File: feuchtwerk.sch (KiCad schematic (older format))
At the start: 47 parts, among them P1 CONN_01X04, P2 CONN_01X08, P3 CONN_01X08, U1 STM32F042K6Tx, U2 HDC1080, U3 MCP1754ST-3302E/MB, U4 MCP1754ST-5002E/MB, U5 TJA1051/3, X1 CON_SWD, Y1 8MHz

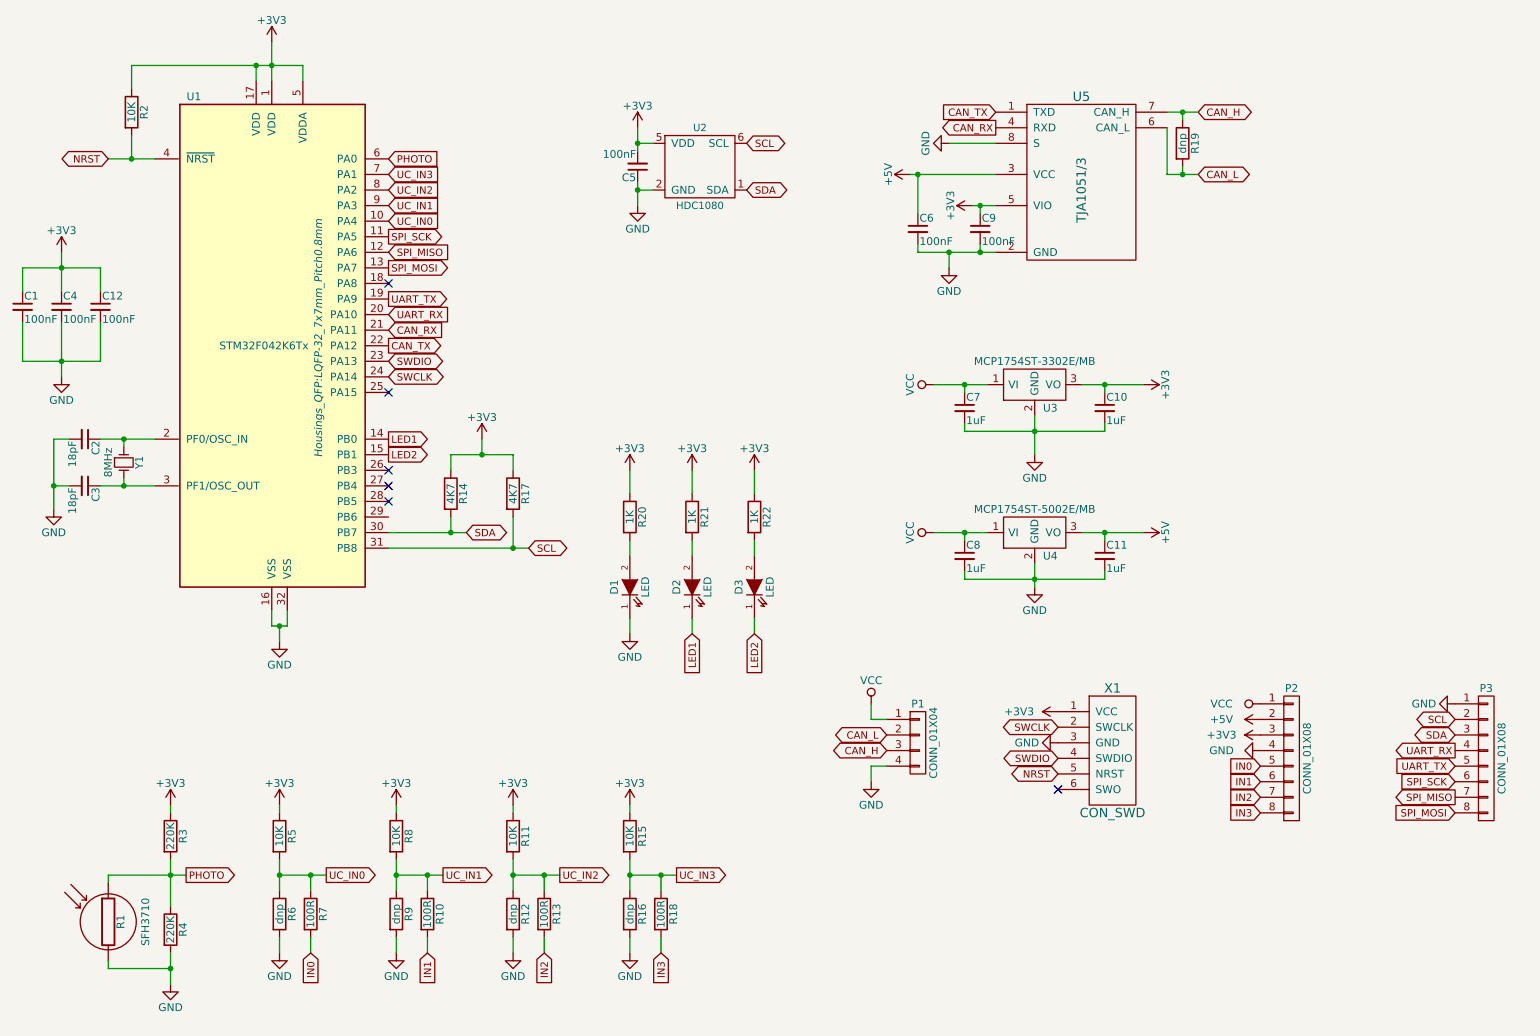
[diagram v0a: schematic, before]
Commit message: fix wrong light transistor setup, add bmp280 air pressure sensor
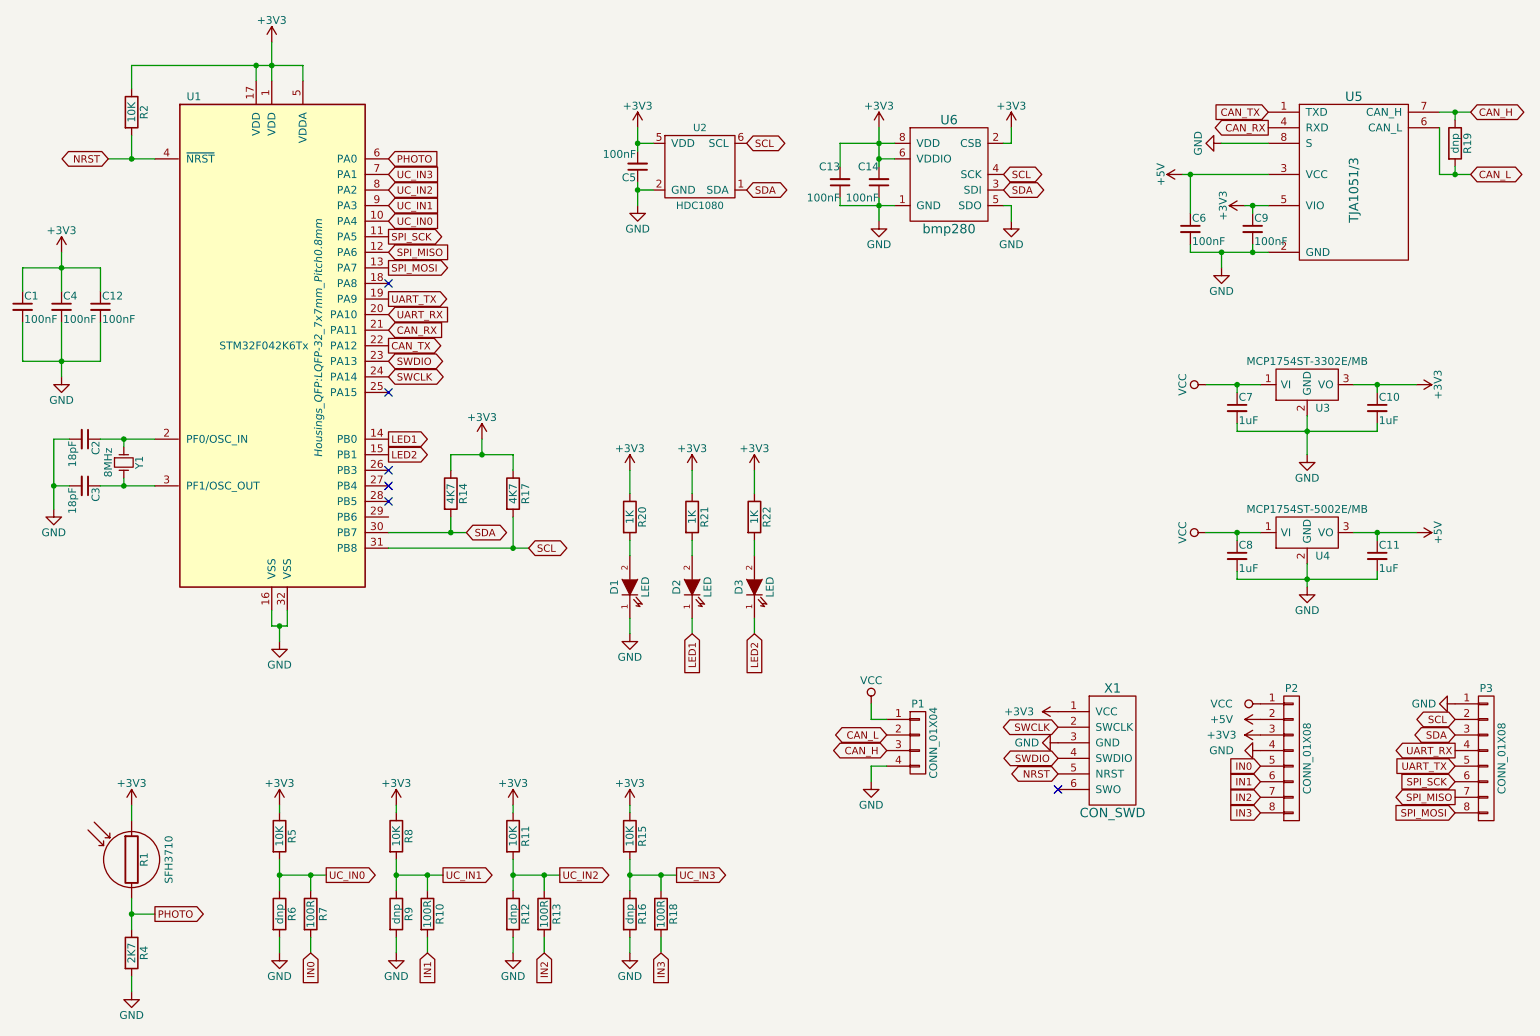
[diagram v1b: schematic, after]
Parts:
- removed R3: 220K, Resistors_SMD:R_0603, symbol R
- added C13, C14: 100nF, Capacitors_SMD:C_0603, symbol C_Small
- added U6: bmp280, bma280:bmp280, symbol bmp280
- R4: value 220K -> 2K7
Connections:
- net +3V3: now also R1.1, C13.2, C14.2, U6.2 (CSB), U6.6 (VDDIO), U6.8 (VDD)
- net GND: now also C13.1, C14.1, U6.1 (GND), U6.5 (SDO), U6.7 (GND); no longer R1.2
- net PHOTO: now also R1.2; no longer R1.1
- net SCL: now also U6.4 (SCK)
- net SDA: now also U6.3 (SDI)
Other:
- moved on the sheet: C10, C11, C6, C7, C8, C9, R1, R19, R4, U3, U4, U5
